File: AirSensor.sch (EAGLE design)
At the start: 27 parts, among them J1 battery Output 7.4V, U1 ATSAMD21G18A-AU, Y1 32.768kHz

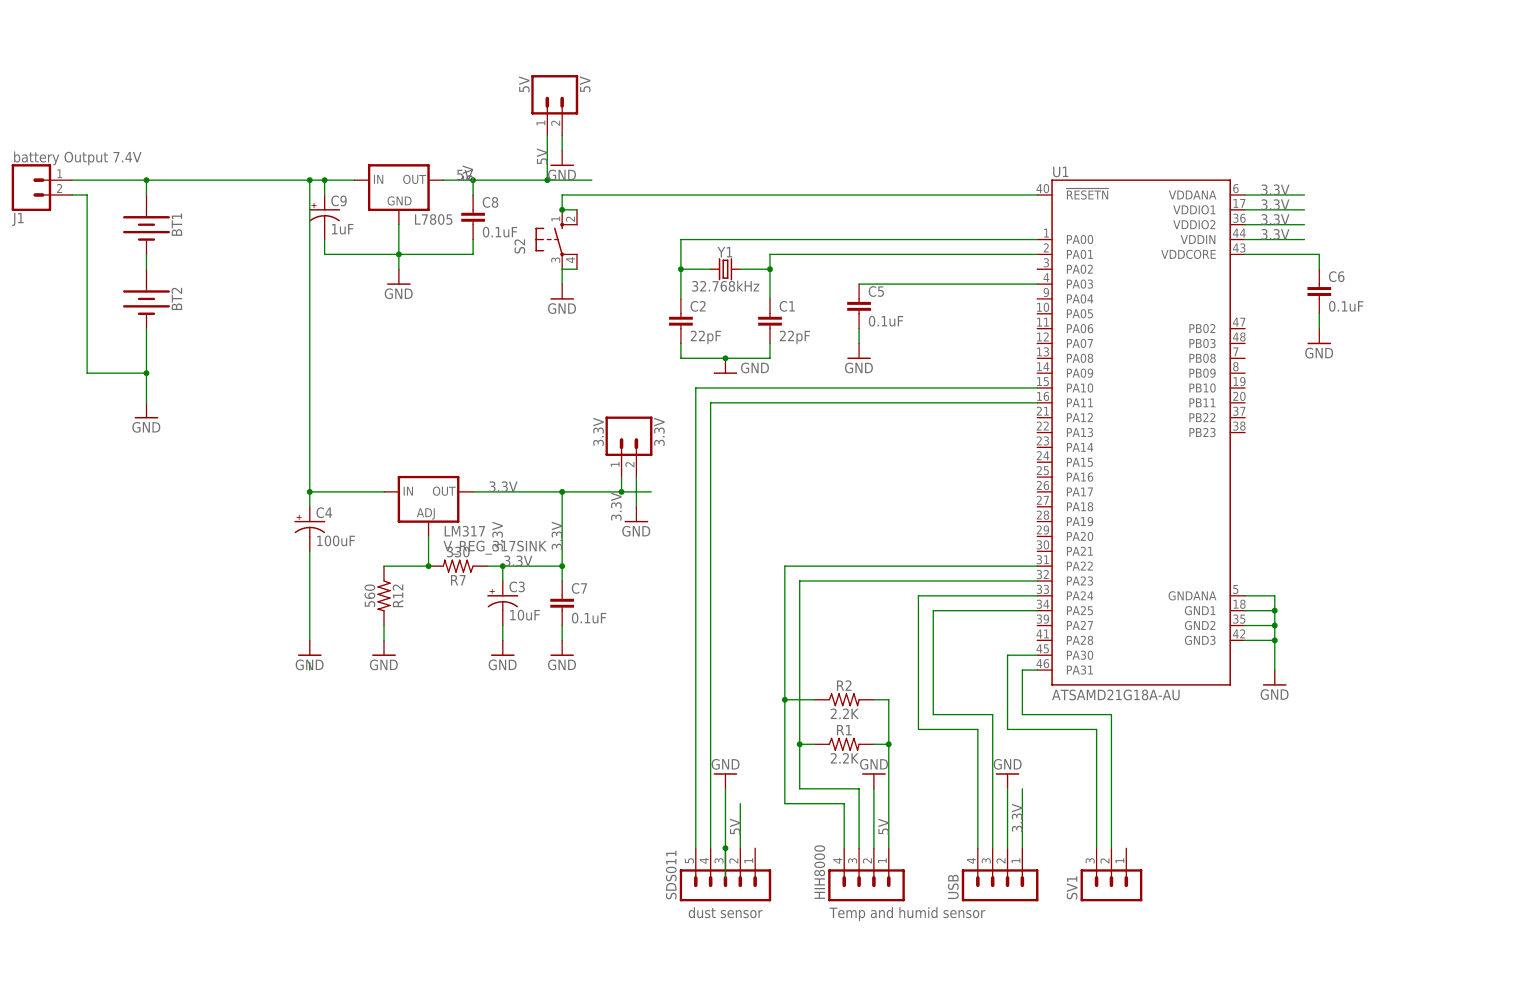
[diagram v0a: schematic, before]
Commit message: added all 3 schematics en all 3 PCB deigns
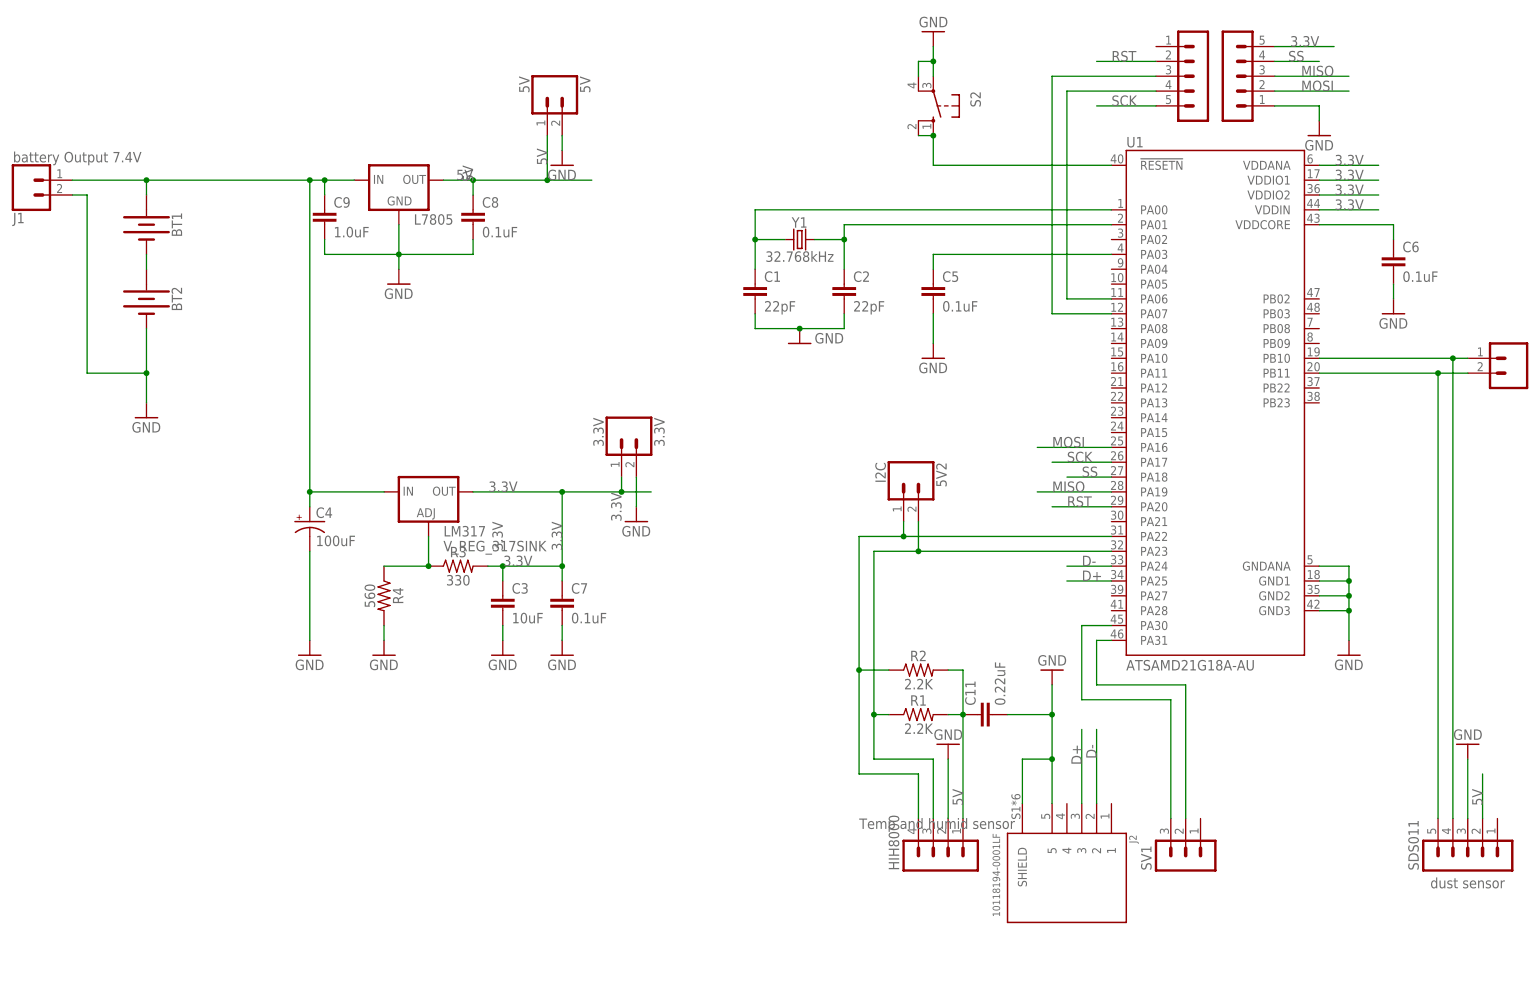
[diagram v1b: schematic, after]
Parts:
- removed R12: 560, SparkFun-Resistors:1KOHM-VERT-1/4W-1%
- removed R7: 330, SparkFun-Resistors:1KOHM-VERT-1/4W-1%
- removed USB: (no value), con-lstb:MA04-1
- added 5V1: UART, SparkFun-Connectors:CONN_02
- added 5V2: I2C, SparkFun-Connectors:CONN_02
- added C11: 0.22uF, SparkFun-Capacitors:1.0UF-0805-25V-10%
- added J2: 10118194-0001LF, 10118194-0001LF:10118194-0001LF
- added R3: 330, SparkFun-Resistors:0.3OHM-0805-1/8W-1%
- added R4: 560, SparkFun-Resistors:0.3OHM-0805-1/8W-1%
- added RFM95W: LoRa1, con-lstb:MA05-1
- added RFM95W_2: LoRa_2, con-lstb:MA05-1
- C1, C2: device capacitor-wima:C2.5/5 -> SparkFun-Capacitors:1.0UF-0805-25V-10%
- C3: device SparkFun-Capacitors:10UF-POLAR-RADIAL-2.5MM-25V-20% -> SparkFun-Capacitors:1.0UF-0805-25V-10%
- C5, C6, C7, C8: device SparkFun-Capacitors:0.1UF-KIT-EZ-50V-20% -> SparkFun-Capacitors:1.0UF-0805-25V-10%
- C9: value 1uF -> 1.0uF; device SparkFun-Capacitors:10UF-POLAR-RADIAL-2.5MM-25V-20% -> SparkFun-Capacitors:1.0UF-0805-25V-(+80/-20%)
- R1, R2: device SparkFun-Resistors:1KOHM-VERT-1/4W-1% -> SparkFun-Resistors:0.3OHM-0805-1/8W-1%
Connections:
- removed net N$13: U1.PA25, USB.3
- new net D+: J2.3, U1.PA25
- new net D-: J2.2, U1.PA24
- new net MISO: RFM95W_2.3, U1.PA19
- new net MOSI: RFM95W_2.2, U1.PA16
- new net N$27: RFM95W.3, U1.PA07
- new net RST: RFM95W.2, U1.PA20
- new net SCK: RFM95W.5, U1.PA17
- new net SS: RFM95W_2.4, U1.PA18
- net 3.3V: now also C3.1, R3.2, RFM95W_2.5; no longer C3.+, R7.1, USB.1
- net 5V: now also C11.1
- net GND: now also C11.2, C3.2, C9.2, J2.5, J2.SHIELD, R4.2, RFM95W_2.1; no longer C3.-, C9.-, R12.2, USB.2
- net N$1: now also 5V2.2
- net N$11: now also C9.1; no longer C9.+
- net N$12: now also 5V2.1
- net N$14: now also RFM95W.4, U1.PA06; no longer U1.PA24, USB.4
- net N$2: now also 5V1.1, SDS011.4, U1.PB10; no longer SDS011.5, U1.PA10
- net N$3: now also 5V1.2, SDS011.5, U1.PB11; no longer SDS011.4, U1.PA11
- net N$6: now also C1.1; no longer C2.1
- net N$7: now also R3.1, R4.1; no longer R12.1, R7.2
- net N$9: now also C2.1; no longer C1.1
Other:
- moved on the sheet: C1, C2, C5, C6, HIH8000, R1, R2, S2, SDS011, SV1, U1, Y1

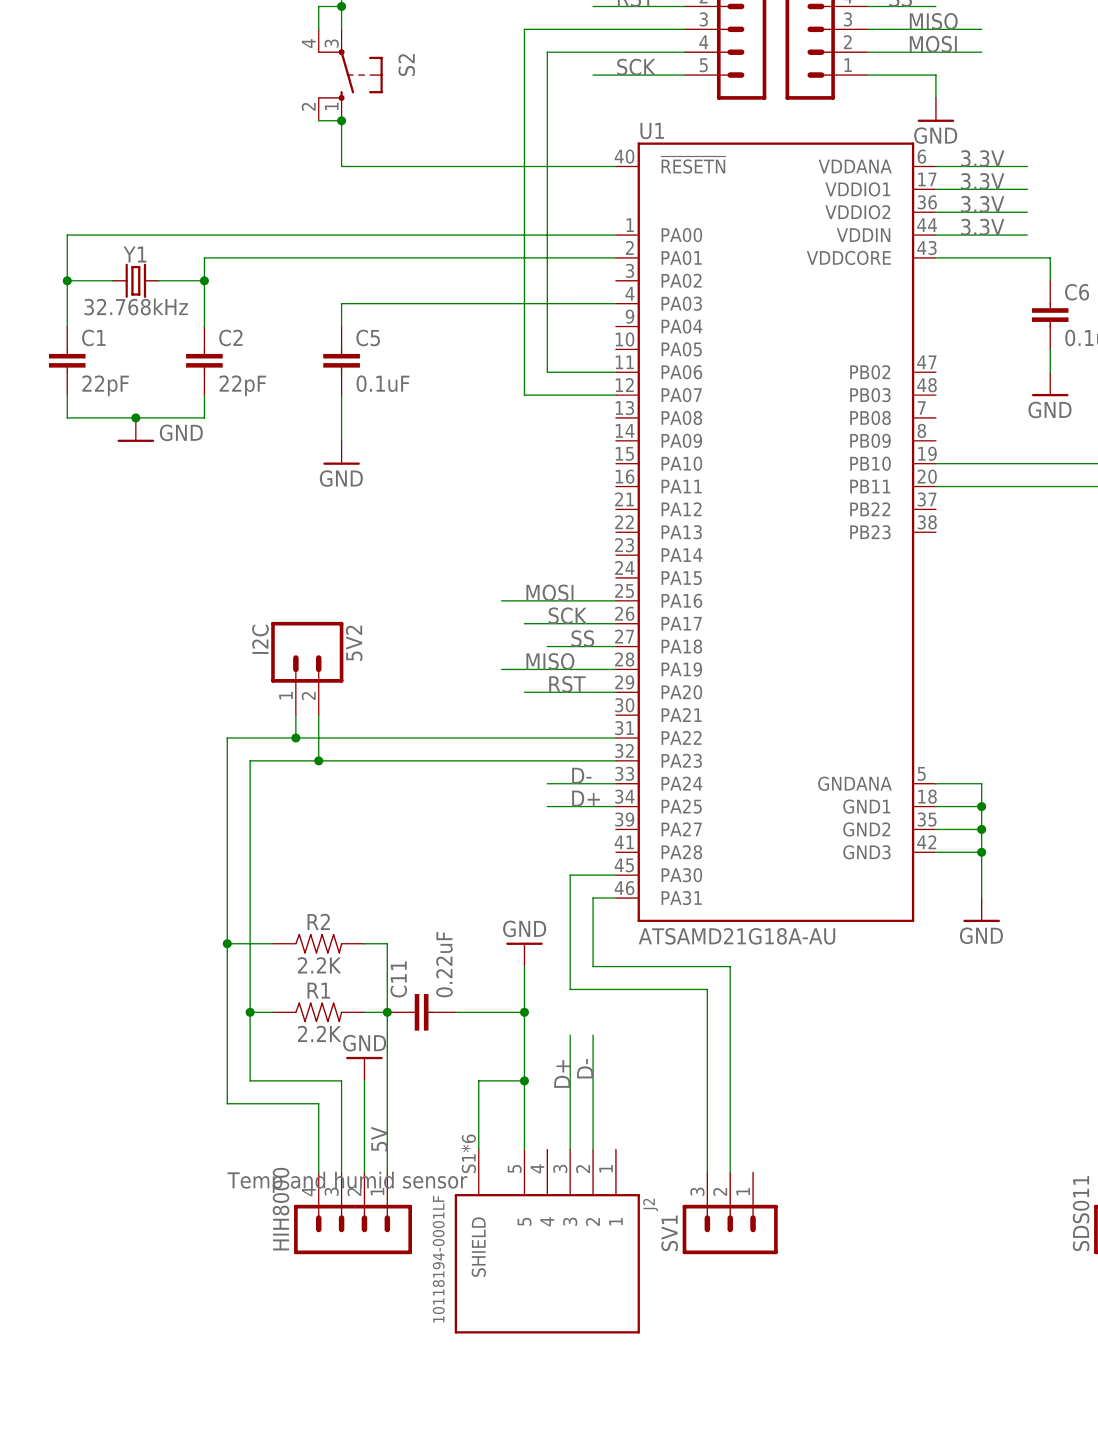
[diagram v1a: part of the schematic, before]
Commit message: added JTAG schematic and PCB  + all pictures
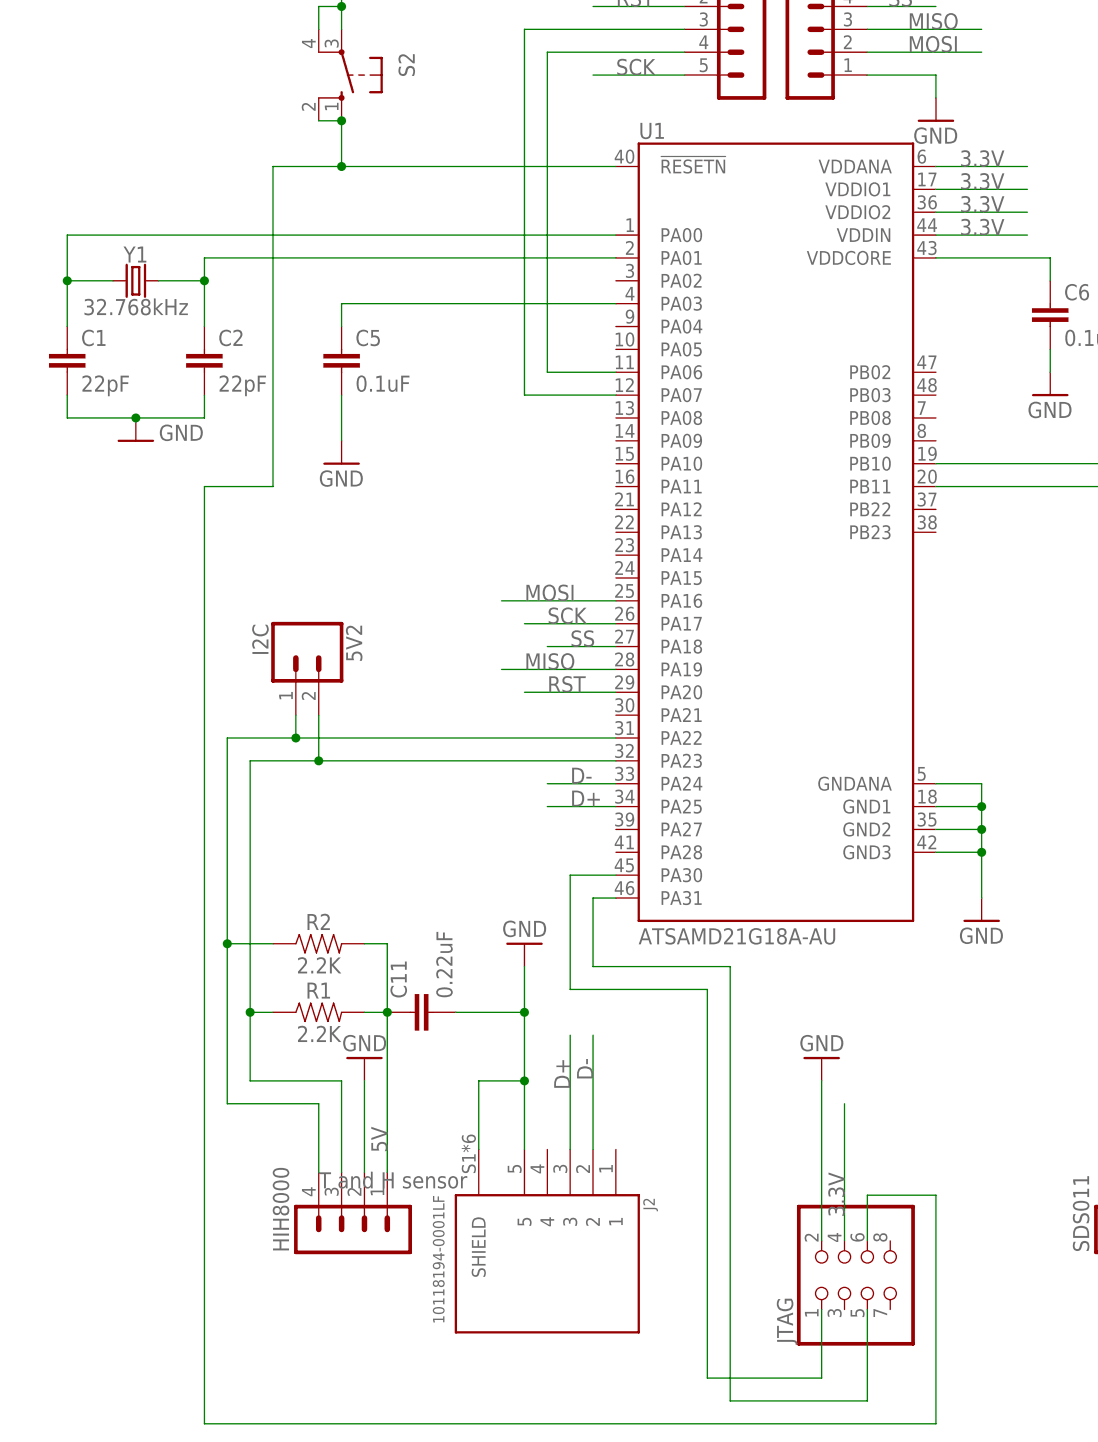
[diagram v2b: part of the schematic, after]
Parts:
- removed SV1: (no value), con-lstb:MA03-1
- added JTAG: (no value), adafruit:PINHD-2X4
- HIH8000: value Temp and humid sensor -> T and H sensor
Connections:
- net 3.3V: now also JTAG.4
- net GND: now also JTAG.2
- net N$10: now also JTAG.6
- net N$15: now also JTAG.1; no longer SV1.3
- net N$16: now also JTAG.5; no longer SV1.2
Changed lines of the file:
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@@
 <part name="Y1" library="SparkFun-Clocks" library_urn="urn:adsk.eagle:library:511" deviceset="CRYSTAL-32.768KHZ" device="SMD-3.2X1.5" package3d_urn="urn:adsk.eagle:package:37548/1" value="32.768kHz"/>
 <part name="SDS011" library="con-lstb" library_urn="urn:adsk.eagle:library:162" deviceset="MA05-1" device="" package3d_urn="urn:adsk.eagle:package:8332/1" value="dust sensor"/>
-<part name="HIH8000" library="con-lstb" library_urn="urn:adsk.eagle:library:162" deviceset="MA04-1" device="" package3d_urn="urn:adsk.eagle:package:8337/1" value="Temp and humid sensor"/>
+<part name="HIH8000" library="con-lstb" library_urn="urn:adsk.eagle:library:162" deviceset="MA04-1" device="" package3d_urn="urn:adsk.eagle:package:8337/1" value="T and H sensor"/>
 <part name="GND8" library="SparkFun-Aesthetics" deviceset="GND" device=""/>
 <part name="GND11" library="SparkFun-Aesthetics" deviceset="GND" device=""/>
-<part name="SV1" library="con-lstb" library_urn="urn:adsk.eagle:library:162" deviceset="MA03-1" device="" package3d_urn="urn:adsk.eagle:package:8339/1"/>
 <part name="RFM95W" library="con-lstb" library_urn="urn:adsk.eagle:library:162" deviceset="MA05-1" device="" package3d_urn="urn:adsk.eagle:package:8332/1" value="LoRa1"/>
 <part name="RFM95W_2" library="con-lstb" library_urn="urn:adsk.eagle:library:162" deviceset="MA05-1" device="" package3d_urn="urn:adsk.eagle:package:8332/1" value="LoRa_2"/>
@@
 <part name="R2" library="SparkFun-Resistors" library_urn="urn:adsk.eagle:library:532" deviceset="0.3OHM" device="-0805-1/8W-1%" package3d_urn="urn:adsk.eagle:package:39651/1" value="2.2K"/>
 <part name="C11" library="SparkFun-Capacitors" library_urn="urn:adsk.eagle:library:510" deviceset="1.0UF" device="-0805-25V-10%" package3d_urn="urn:adsk.eagle:package:37429/1" value="0.22uF"/>
+<part name="JTAG" library="adafruit" library_urn="urn:adsk.eagle:library:420" deviceset="PINHD-2X4" device="" package3d_urn="urn:adsk.eagle:package:6240893/1"/>
+<part name="GND18" library="SparkFun-Aesthetics" deviceset="GND" device=""/>
 </parts>
 <sheets>
@@
 <attribute name="VALUE" x="27.94" y="48.26" size="1.778" layer="96" rot="R180"/>
 </instance>
-<instance part="SV1" gate="G$1" x="48.26" y="12.7" smashed="yes" rot="R90">
-<attribute name="VALUE" x="55.88" y="11.43" size="1.778" layer="96" rot="R90"/>
-<attribute name="NAME" x="42.418" y="11.43" size="1.778" layer="95" rot="R90"/>
-</instance>
 <instance part="RFM95W" gate="G$1" x="50.8" y="147.32" smashed="yes" rot="R180"/>
 <instance part="RFM95W_2" gate="G$1" x="55.88" y="147.32" smashed="yes"/>
@@
 <attribute name="NAME" x="12.319" y="39.624" size="1.778" layer="95" font="vector" rot="R90"/>
 <attribute name="VALUE" x="17.399" y="39.624" size="1.778" layer="96" font="vector" rot="R90"/>
+</instance>
+<instance part="JTAG" gate="A" x="63.5" y="7.62" smashed="yes" rot="R90">
+<attribute name="NAME" x="55.245" y="1.27" size="1.778" layer="95" rot="R90"/>
+<attribute name="VALUE" x="71.12" y="1.27" size="1.778" layer="96" rot="R90"/>
+</instance>
+<instance part="GND18" gate="1" x="58.42" y="33.02" smashed="yes" rot="R180">
+<attribute name="VALUE" x="60.96" y="35.56" size="1.778" layer="96" rot="R180"/>
 </instance>
 </instances>
@@
 <junction x="5.08" y="149.86"/>
 </segment>
+<segment>
+<pinref part="GND18" gate="1" pin="GND"/>
+<pinref part="JTAG" gate="A" pin="2"/>
+<wire x1="58.42" y1="30.48" x2="58.42" y2="12.7" width="0.1524" layer="91"/>
+</segment>
 </net>
 <net name="N$7" class="0">
@@
 <wire x1="5.08" y1="132.08" x2="35.56" y2="132.08" width="0.1524" layer="91"/>
 <pinref part="U1" gate="G$1" pin="!RESETN"/>
+<pinref part="JTAG" gate="A" pin="6"/>
+<wire x1="63.5" y1="12.7" x2="63.5" y2="17.78" width="0.1524" layer="91"/>
+<wire x1="63.5" y1="17.78" x2="71.12" y2="17.78" width="0.1524" layer="91"/>
+<wire x1="71.12" y1="17.78" x2="71.12" y2="-7.62" width="0.1524" layer="91"/>
+<wire x1="71.12" y1="-7.62" x2="-10.16" y2="-7.62" width="0.1524" layer="91"/>
+<wire x1="-10.16" y1="-7.62" x2="-10.16" y2="96.52" width="0.1524" layer="91"/>
+<wire x1="-10.16" y1="96.52" x2="-2.54" y2="96.52" width="0.1524" layer="91"/>
+<wire x1="-2.54" y1="96.52" x2="-2.54" y2="132.08" width="0.1524" layer="91"/>
+<wire x1="-2.54" y1="132.08" x2="5.08" y2="132.08" width="0.1524" layer="91"/>
+<junction x="5.08" y="132.08"/>
 </segment>
 </net>
@@
 <label x="71.12" y="152.4" size="1.778" layer="95" align="bottom-right"/>
 </segment>
+<segment>
+<pinref part="JTAG" gate="A" pin="4"/>
+<wire x1="60.96" y1="12.7" x2="60.96" y2="27.94" width="0.1524" layer="91"/>
+<label x="60.96" y="20.32" size="1.778" layer="95" rot="R90" align="bottom-right"/>
+</segment>
 </net>
 <net name="N$1" class="0">
@@
 <net name="N$15" class="0">
 <segment>
-<pinref part="SV1" gate="G$1" pin="3"/>
-<wire x1="45.72" y1="20.32" x2="45.72" y2="40.64" width="0.1524" layer="91"/>
 <wire x1="45.72" y1="40.64" x2="30.48" y2="40.64" width="0.1524" layer="91"/>
 <wire x1="30.48" y1="40.64" x2="30.48" y2="53.34" width="0.1524" layer="91"/>
 <pinref part="U1" gate="G$1" pin="PA30"/>
 <wire x1="30.48" y1="53.34" x2="35.56" y2="53.34" width="0.1524" layer="91"/>
+<wire x1="45.72" y1="40.64" x2="45.72" y2="-2.54" width="0.1524" layer="91"/>
+<wire x1="45.72" y1="-2.54" x2="58.42" y2="-2.54" width="0.1524" layer="91"/>
+<pinref part="JTAG" gate="A" pin="1"/>
+<wire x1="58.42" y1="-2.54" x2="58.42" y2="5.08" width="0.1524" layer="91"/>
 </segment>
 </net>
@@
 <wire x1="33.02" y1="50.8" x2="33.02" y2="43.18" width="0.1524" layer="91"/>
 <wire x1="33.02" y1="43.18" x2="48.26" y2="43.18" width="0.1524" layer="91"/>
-<pinref part="SV1" gate="G$1" pin="2"/>
-<wire x1="48.26" y1="43.18" x2="48.26" y2="20.32" width="0.1524" layer="91"/>
-</segment>
-</net>
+<wire x1="48.26" y1="43.18" x2="48.26" y2="-5.08" width="0.1524" layer="91"/>
+<wire x1="48.26" y1="-5.08" x2="63.5" y2="-5.08" width="0.1524" layer="91"/>
+<pinref part="JTAG" gate="A" pin="5"/>
+<wire x1="63.5" y1="-5.08" x2="63.5" y2="5.08" width="0.1524" layer="91"/>
+</segment>
+</net>
